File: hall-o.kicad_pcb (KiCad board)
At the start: 2 copper layers, 44.2 x 17.8 mm, 16 parts, among them P1 CONN_01X04, Q1 BC848, U1 ss495b, U2 LM258D

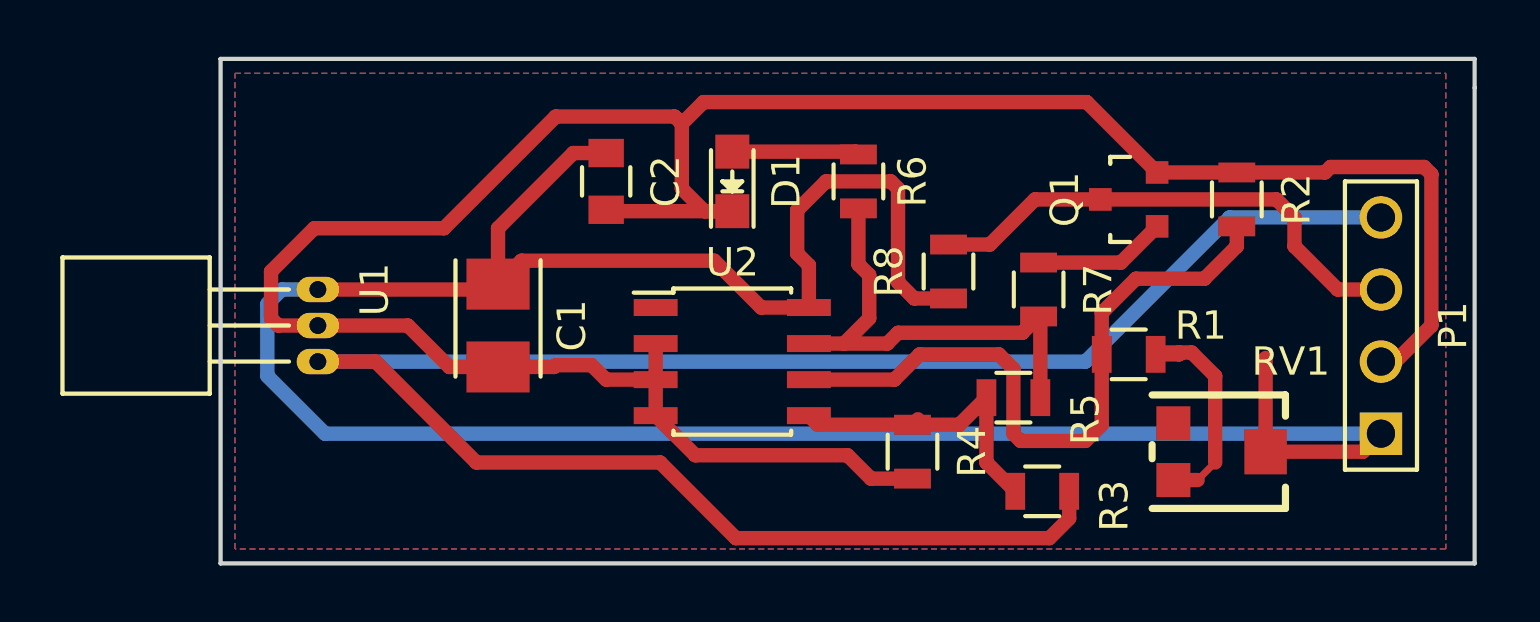
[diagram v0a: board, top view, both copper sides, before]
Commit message: single sided, rerouted
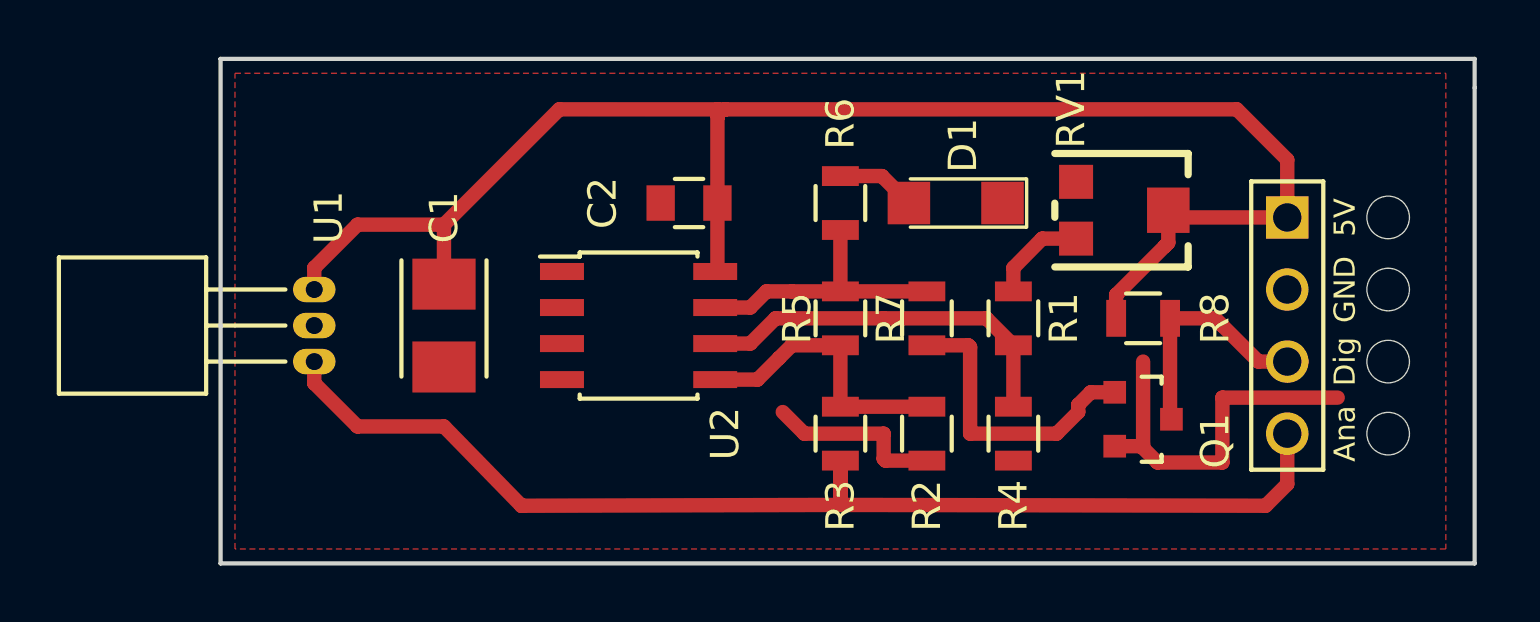
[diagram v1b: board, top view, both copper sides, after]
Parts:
- added 5V: MountingHole_2.2mm_M2, Mounting_Holes:MountingHole_2.2mm_M2, F.Cu at (159.0, 99.1)
- added Ana: MountingHole_2.2mm_M2, Mounting_Holes:MountingHole_2.2mm_M2, F.Cu at (159.0, 106.7)
- added Dig: MountingHole_2.2mm_M2, Mounting_Holes:MountingHole_2.2mm_M2, F.Cu at (159.0, 104.1)
- added GND: MountingHole_2.2mm_M2, Mounting_Holes:MountingHole_2.2mm_M2, F.Cu at (159.0, 101.6)
- C2: value 100nf -> 100n
- D1: footprint LEDs:LED_0805 -> LEDs:LED_1206
- P1: value CONN_01X04 -> CONN
- R1, R4, R8: value 10k -> 10K
- R2: value 22k -> 22K
- R5: value 1m -> 1M
- R7: value 1k -> 1K
- moved R2 11.4 mm to (145.8, 106.7), turned to 90 degrees
- moved RV1 9.17 mm to (149.6, 98.8)
- moved D1 7.91 mm to (143.8, 98.6), turned to 180 degrees
- moved Q1 7.76 mm to (150.4, 106.2), turned to 270 degrees
- moved R3 7.40 mm to (139.7, 106.7), turned to 90 degrees
- moved R8 7.05 mm to (150.4, 102.6), turned to 0 degrees
- moved R5 6.71 mm to (139.7, 102.6), turned to 270 degrees
- moved R1 4.26 mm to (145.8, 102.6), turned to 90 degrees
- moved R7 4.07 mm to (142.7, 102.6), turned to 90 degrees
- moved U2 3.54 mm to (132.6, 102.9)
- moved P1 3.30 mm to (155.4, 102.9), turned to 270 degrees
- moved C2 3.02 mm to (134.4, 98.6), turned to 180 degrees
- moved C1 1.91 mm to (125.7, 102.9)
- moved R6 0.99 mm to (139.7, 98.6)
- moved R4 0.81 mm to (142.7, 106.7)
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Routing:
- net /GND: track 89.9 -> 19.7 mm
- net /+5V: track 90.5 -> 57.4 mm
- net /SIG: track 69.9 -> 42.1 mm
- net Net-(R1-Pad1): track 23.9 -> 13.4 mm
- net /STOP: track 17.8 -> 8.85 mm
- net Net-(R5-Pad1): track 16.7 -> 9.86 mm
- net Net-(Q1-Pad1): track 4.70 -> 10.9 mm
- net Net-(R1-Pad2): track 7.79 -> 3.47 mm
- net Net-(D1-Pad2): track 4.49 -> 2.81 mm
- net Net-(R3-Pad2): track 10.8 -> 10.1 mm
- removed copper zone on B.Cu, net /+5V

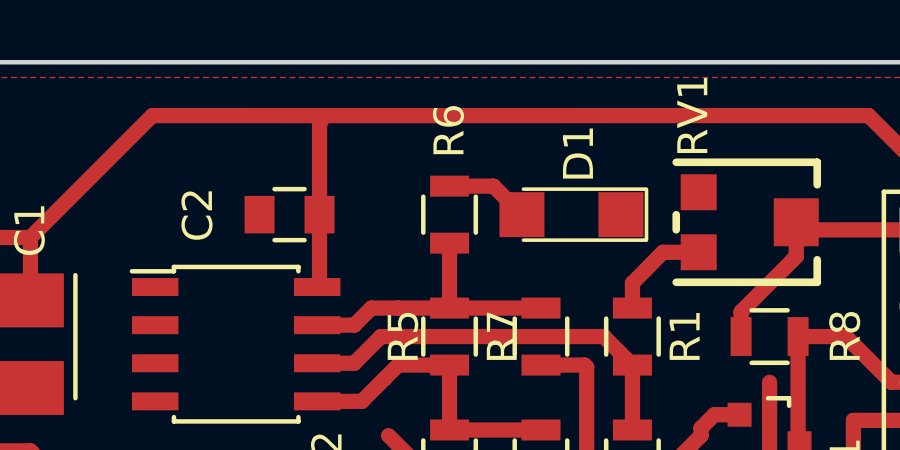
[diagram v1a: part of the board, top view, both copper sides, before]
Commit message: update renderings
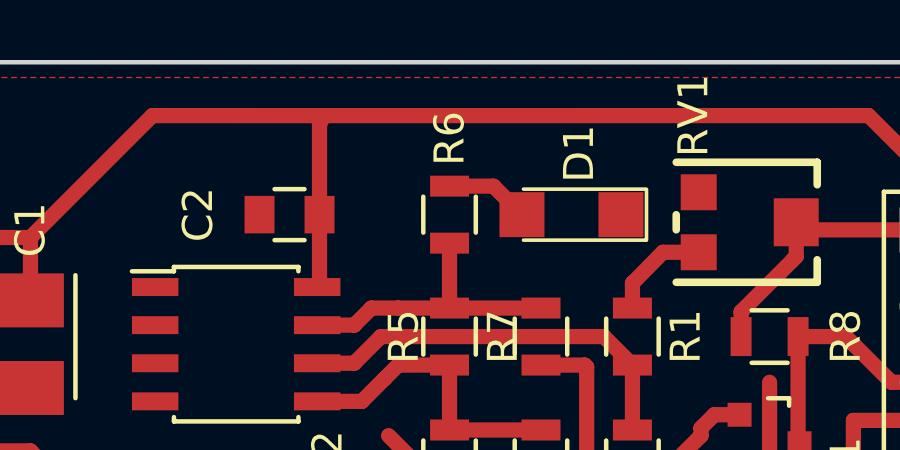
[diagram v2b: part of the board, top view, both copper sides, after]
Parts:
- 5V, Ana, Dig, GND: value MountingHole_2.2mm_M2 -> (none)
- U1: value ss495b -> SS495B
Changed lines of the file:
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@@
     (links 31)
     (no_connects 0)
-    (area 109.183 93.396999 175.065 114.459143)
+    (area 117.780999 93.396999 162.127001 111.327001)
     (thickness 1.6)
     (drawings 5)
@@
   )
   (setup
-    (last_trace_width 0.508)
+    (last_trace_width 0.25)
     (user_trace_width 0.381)
     (user_trace_width 0.508)
@@
       (effects (font (size 0.75 0.75) (thickness 0.15)))
     )
-    (fp_text value MountingHole_2.2mm_M2 (at 10.668 0.762 90) (layer F.Fab) hide
+    (fp_text value "" (at 10.668 0.762 90) (layer F.Fab) hide
       (effects (font (size 1 1) (thickness 0.15)))
     )
@@
       (effects (font (size 0.75 0.75) (thickness 0.15)))
     )
-    (fp_text value MountingHole_2.2mm_M2 (at 14.986 3.048 90) (layer F.Fab) hide
+    (fp_text value "" (at 14.986 3.048 90) (layer F.Fab) hide
       (effects (font (size 1 1) (thickness 0.15)))
     )
@@
       (effects (font (size 0.75 0.75) (thickness 0.15)))
     )
-    (fp_text value MountingHole_2.2mm_M2 (at 8.89 5.588 90) (layer F.Fab) hide
+    (fp_text value "" (at 8.89 5.588 90) (layer F.Fab) hide
       (effects (font (size 1 1) (thickness 0.15)))
     )
@@
       (effects (font (size 1 1) (thickness 0.15)))
     )
-    (fp_text value 10u/16v (at 3.556 -0.254 360) (layer F.Fab)
+    (fp_text value 10u/16v (at -6.096 -1.524 450) (layer F.Fab)
       (effects (font (size 1 1) (thickness 0.15)))
     )
@@
     (pad 4 thru_hole circle (at 3.81 0 270) (size 1.5 1.5) (drill 1) (layers *.Cu *.Mask F.SilkS)
       (net 5 /SIG))
-    (model ../KiCAD_Libraries/packages3d/rmc/connectors/pin_header_2.54mm_1x4.wrl
+    (model Pin_Headers.3dshapes/Pin_Header_Angled_1x04.wrl
       (at (xyz 0 0 0))
       (scale (xyz 1 1 1))
@@
     (tags "resistor 0805")
     (attr smd)
-    (fp_text reference R6 (at 2.794 0 90) (layer F.SilkS)
+    (fp_text reference R6 (at 2.54 0 90) (layer F.SilkS)
       (effects (font (size 1 1) (thickness 0.15)))
     )
@@
       (rotate (xyz 0 0 0))
     )
+    (model Potentiometers.3dshapes/3312j-1-103e.wrl
+      (at (xyz 0 0 0.05))
+      (scale (xyz 0.9 0.9 0.9))
+      (rotate (xyz -90 0 0))
+    )
   )
   (module TO_SOT_Packages_THT:TO-92_Horizontal1_Inline_Narrow_Oval (layer F.Cu)
@@
       (effects (font (size 1 1) (thickness 0.15)))
     )
-    (fp_text value ss495b (at 0 11 450) (layer F.Fab)
+    (fp_text value SS495B (at -4.318 -1.778 270) (layer F.Fab)
       (effects (font (size 1 1) (thickness 0.15)))
     )
@@
       (effects (font (size 0.75 0.75) (thickness 0.15)))
     )
-    (fp_text value MountingHole_2.2mm_M2 (at 12.954 -2.286 90) (layer F.Fab) hide
-      (effects (font (size 1 1) (thickness 0.15)))
-    )
+    (fp_text value "" (at 12.954 -2.286 90) (layer F.Fab) hide
+      (effects (font (size 1 1) (thickness 0.15)))
+    )

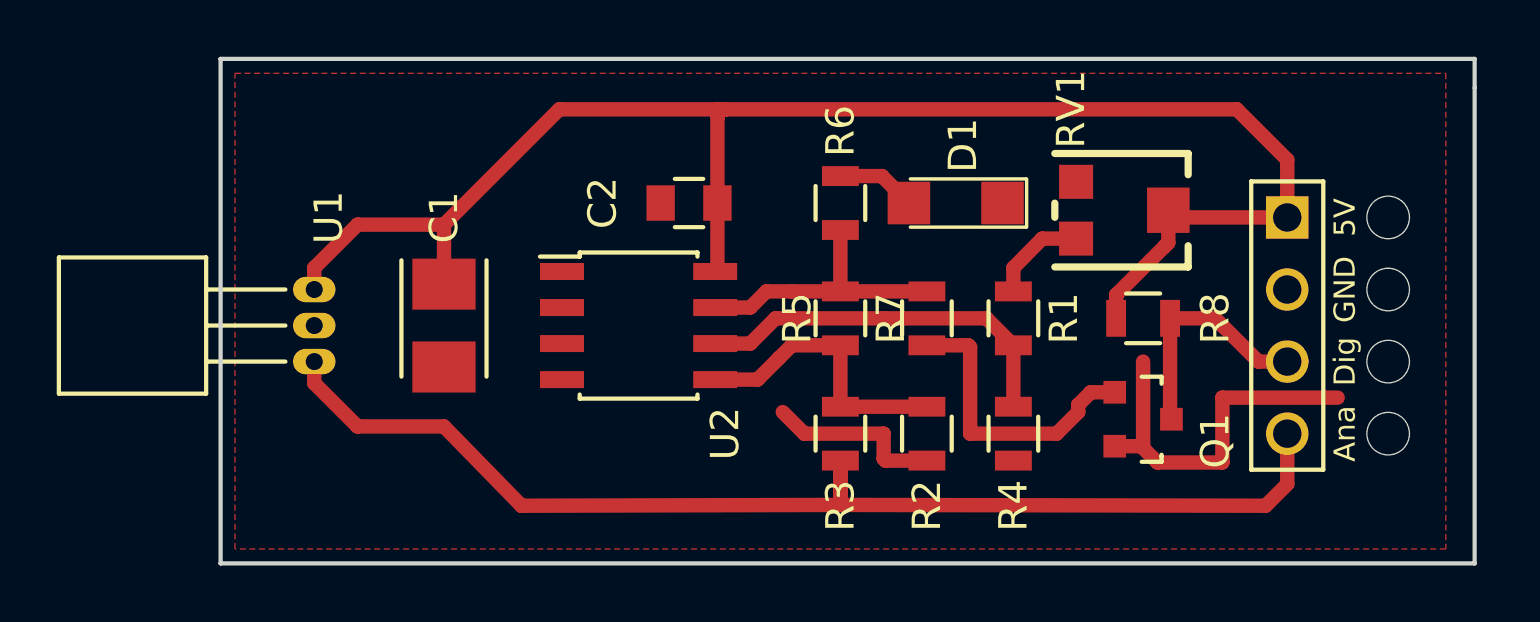
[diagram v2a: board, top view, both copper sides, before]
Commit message: larger tantalum cap
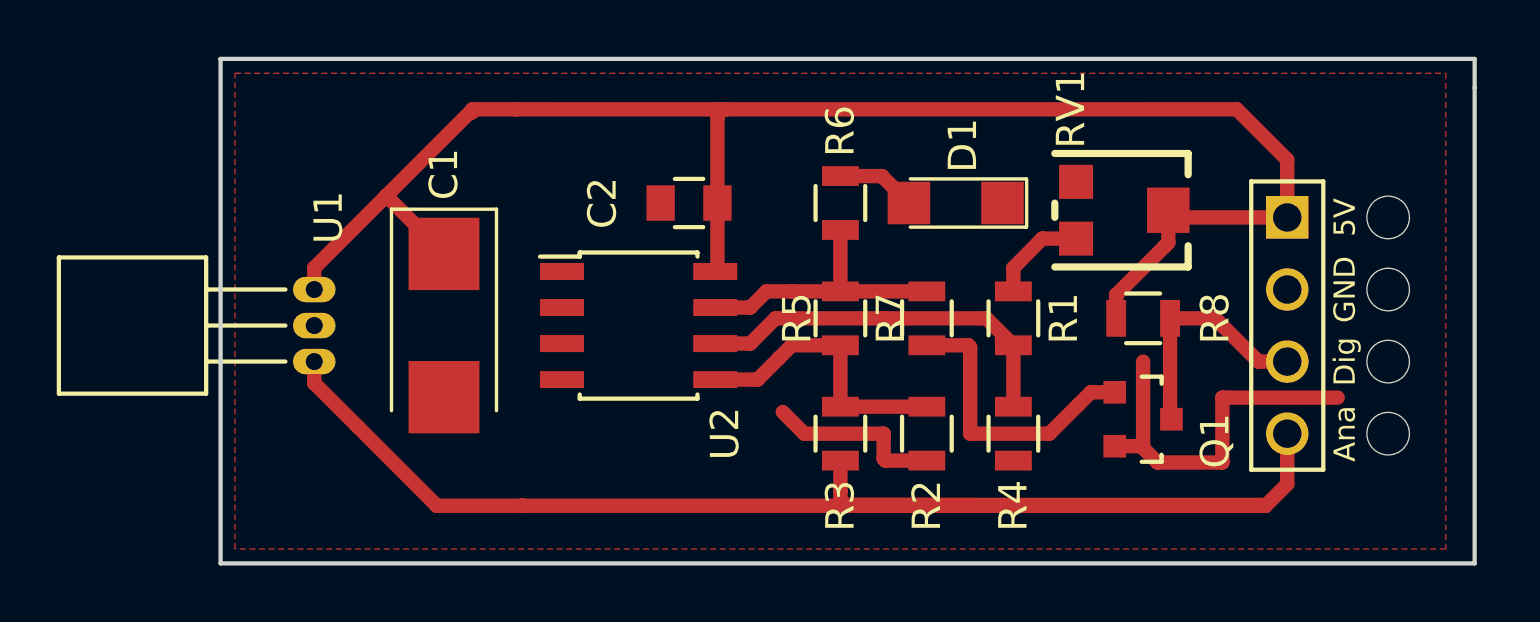
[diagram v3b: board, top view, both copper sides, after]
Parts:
- C1: value 10u/16v -> 10µF/16V; footprint Capacitors_Tantalum_SMD:TantalC_SizeB_EIA-3528_Reflow -> Capacitors_Tantalum_SMD:CP_Tantalum_Case-C_EIA-6032-28_Reflow
- C2: value 100n -> 100nF
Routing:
- net /SIG: track 42.1 -> 70.6 mm
- net /+5V: track 57.4 -> 58.4 mm
